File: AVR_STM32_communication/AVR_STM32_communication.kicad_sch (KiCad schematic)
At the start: 124 parts, among them J1 Goldpin_1x3, J2 Conn_01x02_Pin, J3 Conn_01x02_Socket, J4 Goldpin_1x3, J5 Goldpin, J6 Goldpin, J7 Conn_01x02_Pin, Q1 Q_NMOS, Q10 Q_NMOS, Q11 Q_NMOS, Q12 Q_NMOS, Q13 Q_NMOS, Q14 Q_NMOS, Q15 Q_NMOS, Q16 Q_NMOS, Q17 Q_NMOS, Q18 Q_NMOS, Q2 Q_NMOS, Q3 Q_NMOS, Q4 Q_NMOS, Q5 Q_NMOS, Q6 Q_NMOS, Q7 Q_NMOS, Q8 Q_NMOS, Q9 Q_NMOS, SW1 SW_Push, SW2 SW_Push, U1 ATmega328PB-A, U2 ATmega328PB-A, U3 STM32L010C6Tx, Y1 Crystal, Y2 Crystal

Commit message: Dodanie pierwszego STMa, częściowa konfiguracja jego połączeń.
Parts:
- added C7, C8, C9: C, symbol Device:C
- added JP45: Jumper_3_Open, symbol Jumper:Jumper_3_Open
- added JP46, JP47, JP48, JP50: Goldpin+0805, symbol Jumper:Jumper_2_Small_Open
- added R41: 10k, symbol Device:R
- added SW3: SW_Push, symbol Switch:SW_Push
- added Y3: Crystal, symbol Device:Crystal
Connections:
- net +1V8: now also JP46.1 (A)
- net +3V3: now also JP47.1 (A)
- net +3V6: now also JP48.1 (A)
- net GND: now also U3.23 (VSS), U3.35 (VSS), U3.47 (VSS), U3.8 (VSSA), C7.2, C8.2, C9.2, SW3.1
- net at Q18.S, R40.2: now also JP41.3 (B)
- net at JP14.3 (B): now also Q8.S, R18.2
- net at Q7.S, R17.2: now also JP22.3 (B)
- net at Q17.S, R39.2: now also JP40.3 (B)
- net ADC0_STM32_1: now reaches U3.10 (PA0)
- net ADC1_STM32_1: now reaches U3.11 (PA1)
- net RTC_STM32_1: now reaches U3.12 (PA2)
- net TIM2/32-CH4/2_STM32_1: now reaches U3.13 (PA3)
- net GPIO1_STM32_1: now reaches U3.14 (PA4)
- net TIM2_STM32_1: now reaches U3.15 (PA5)
- net VCC_STM32_1: now reaches U3.24 (VDD)
- net VCC_STM32_1: now also U3.36 (VDD), U3.48 (VDD), JP46.2 (B), JP47.2 (B), JP48.2 (B), JP50.1 (A), R41.1
- net EVENTOUT_STM32_1: now reaches U3.29 (PA8)
- net I2C1_SCL_STM32_1: now reaches U3.30 (PA9)
- net I2C1_SDA_STM32_1: now reaches U3.31 (PA10)
- net SWDIO_STM32_1: now reaches U3.34 (PA13)
- net SWCLK_STM32_1: now reaches U3.37 (PA14)
- net USART2_TX_STM32_1: now reaches U3.42 (PB6)
- net at U3.44 (BOOT0): now also JP45.2 (C)
- net OSC1_STM32_1: now reaches U3.5 (PH0)
- net OSC1_STM32_1: now also C7.1, Y3.1
- net OSC2_STM32_1: now reaches U3.6 (PH1)
- net OSC2_STM32_1: now also C8.1, Y3.2
- net RESET_STM32_1: now reaches U3.7 (NRST)
- net RESET_STM32_1: now also C9.1, R41.2, SW3.2
- net at U3.9 (VDDA): now also JP50.2 (B)
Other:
- note added: "CRYSTAL_AVR_1"
- note added: "CRYSTAL_AVR_2"
- note added: "CRYSTAL_STM32_1"
- note added: "RESET_AVR_1"
- note added: "RESET_AVR_2"
- note added: "RESET_STM32_1"
- note added: "UART_AVR_1"
- note added: "UART_AVR_2"
- moved on the sheet: C1, R1, SW1

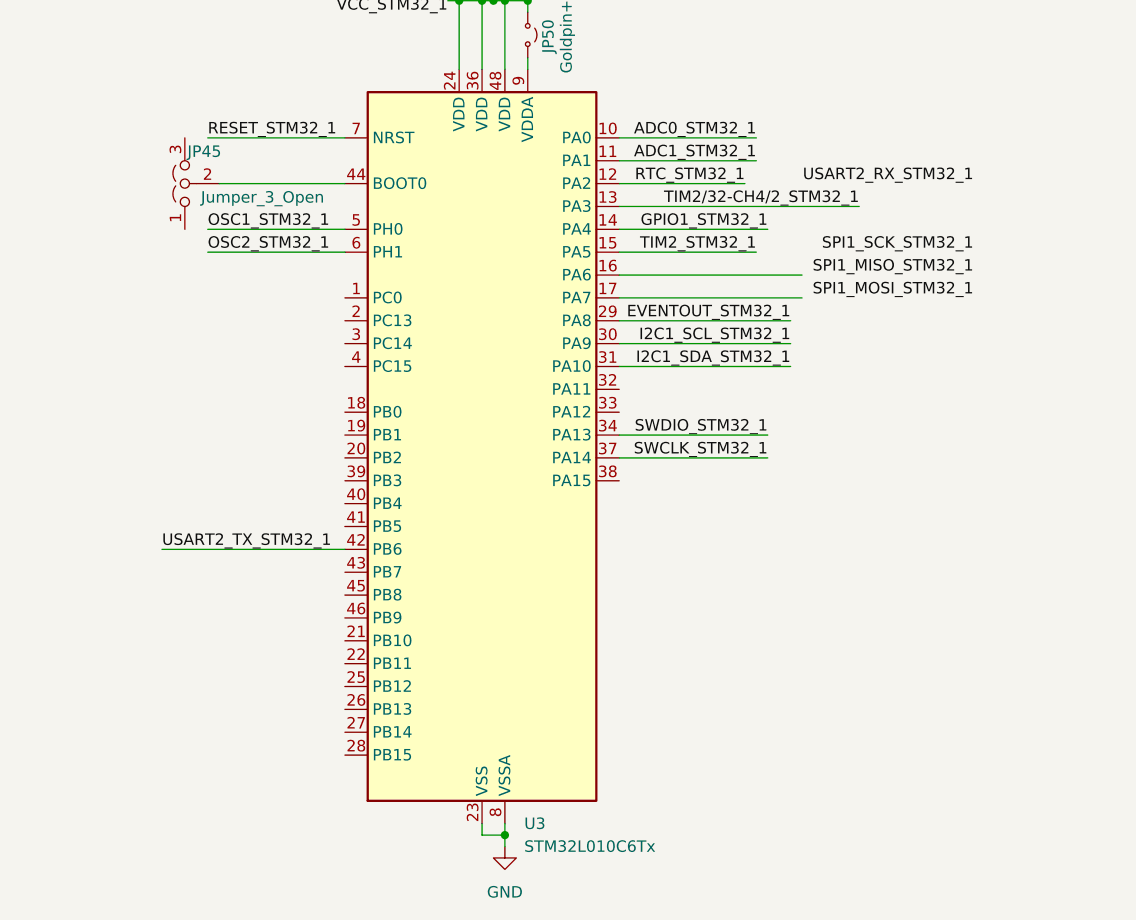
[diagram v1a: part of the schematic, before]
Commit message: Dodanie wszystkich potrzebnych etykiet STM32_1
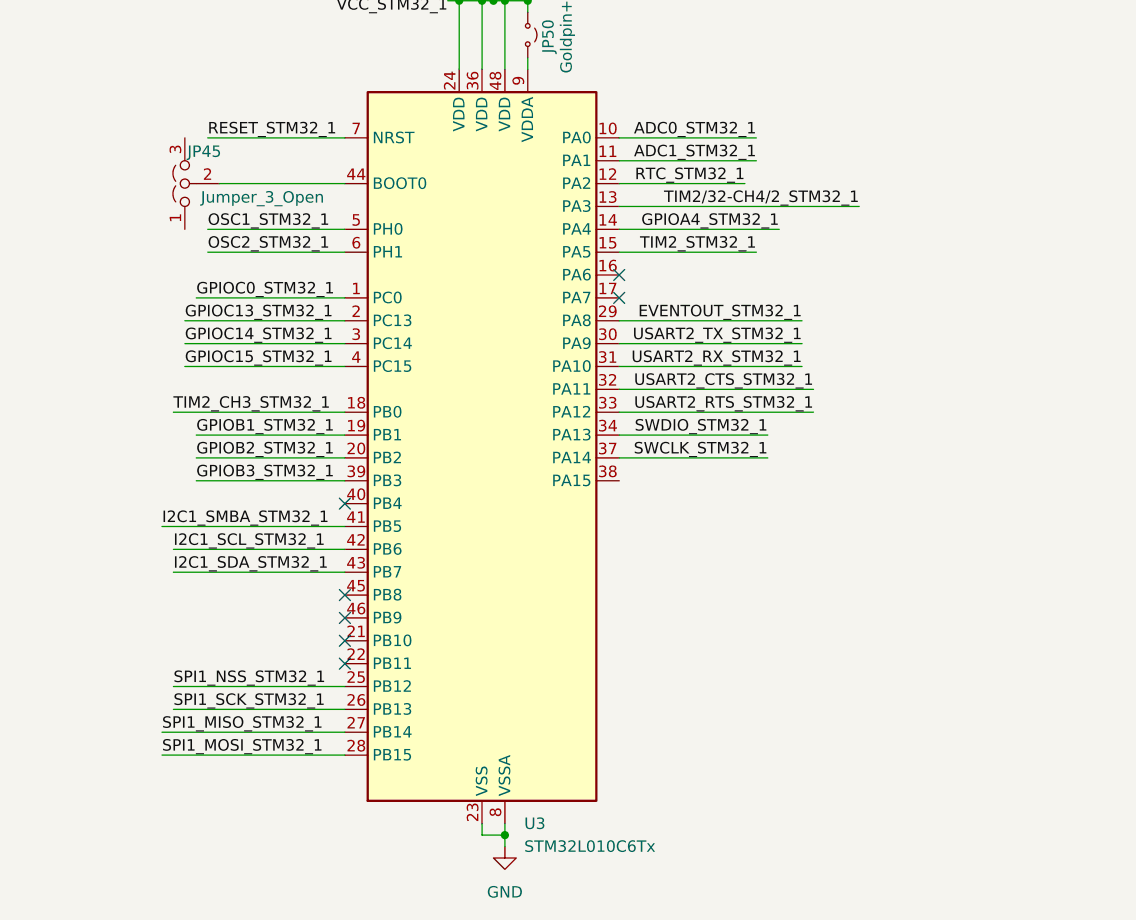
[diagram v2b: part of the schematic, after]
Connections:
- net I2C1_SCL_STM32_1: now also U3.42 (PB6); no longer U3.30 (PA9)
- net I2C1_SDA_STM32_1: now also U3.43 (PB7); no longer U3.31 (PA10)
- net SPI1_MISO_STM32_1: now also U3.27 (PB14)
- net SPI1_MOSI_STM32_1: now also U3.28 (PB15)
- net SPI1_SCK_STM32_1: now also U3.26 (PB13)
- net USART2_RX_STM32_1: now also U3.31 (PA10)
- net USART2_TX_STM32_1: now also U3.30 (PA9); no longer U3.42 (PB6)
- net GPIOC0_STM32_1: now reaches U3.1 (PC0)
- net TIM2_CH3_STM32_1: now reaches U3.18 (PB0)
- net GPIOB1_STM32_1: now reaches U3.19 (PB1)
- net GPIOC13_STM32_1: now reaches U3.2 (PC13)
- net GPIOB2_STM32_1: now reaches U3.20 (PB2)
- net SPI1_NSS_STM32_1: now reaches U3.25 (PB12)
- net GPIOC14_STM32_1: now reaches U3.3 (PC14)
- net USART2_CTS_STM32_1: now reaches U3.32 (PA11)
- net USART2_RTS_STM32_1: now reaches U3.33 (PA12)
- net GPIOB3_STM32_1: now reaches U3.39 (PB3)
- net GPIOC15_STM32_1: now reaches U3.4 (PC15)
- net I2C1_SMBA_STM32_1: now reaches U3.41 (PB5)
- net GPIO1_STM32_1 renamed GPIOA4_STM32_1
- no-connect marks 0 -> 7

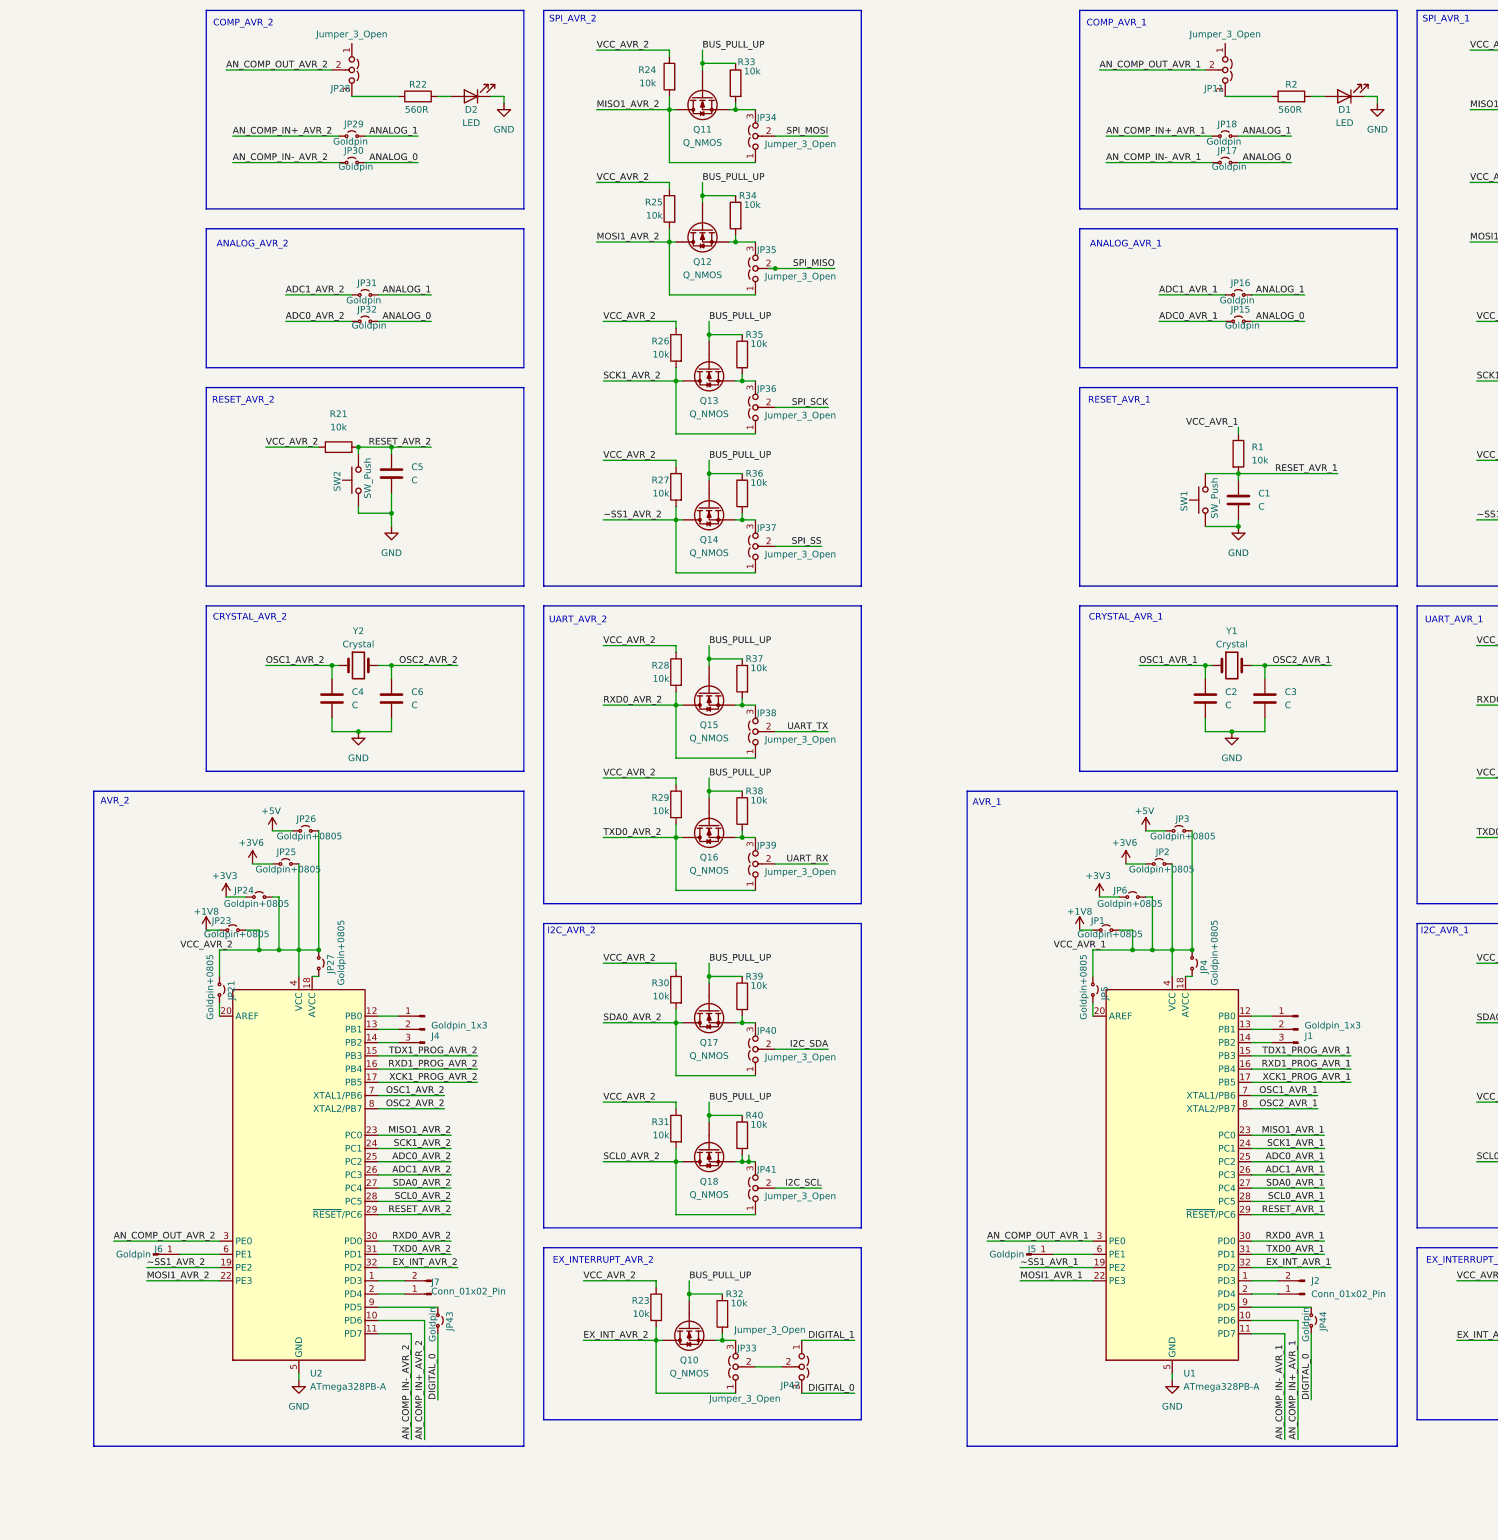
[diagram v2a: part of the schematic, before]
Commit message: Poprawa ułożenia etykiet w AVR
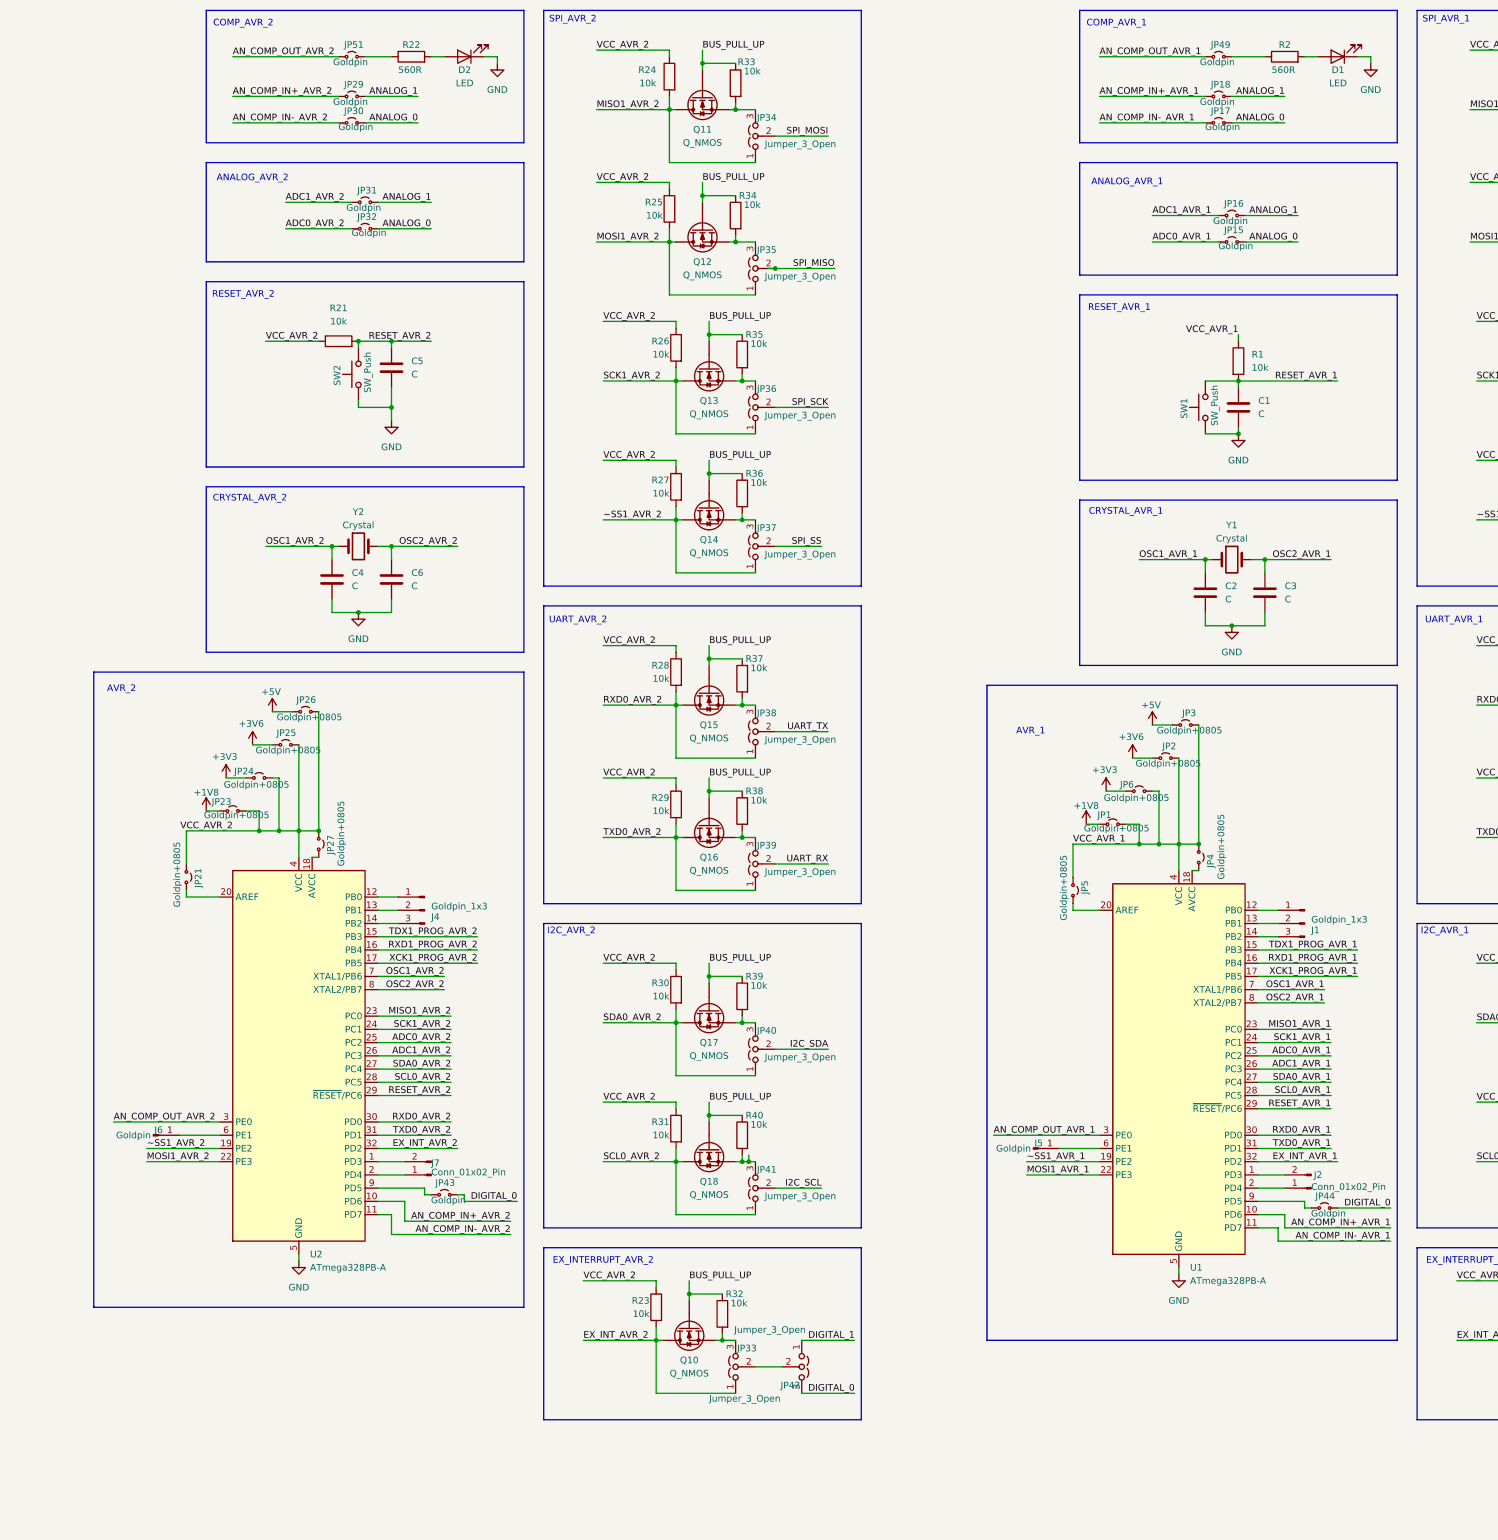
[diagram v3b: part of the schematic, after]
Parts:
- removed JP11, JP28: Jumper_3_Open, symbol Jumper:Jumper_3_Open
- added JP49, JP51: Goldpin, symbol Jumper:Jumper_2_Small_Open
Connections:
- net AN_COMP_OUT_AVR_1: now also JP49.1 (A)
- net AN_COMP_OUT_AVR_2: now also JP51.1 (A)
- net at R2.1: now also JP49.2 (B)
- net at R22.1: now also JP51.2 (B)
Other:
- moved on the sheet: C1, C2, C3, C4, C5, C6, D1, D2, J1, J2, J4, J5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

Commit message: Wydzielenie sekcji zasilania obu AVR jako oddzielny moduł.
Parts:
- removed JP23, JP24, JP25, JP26: Goldpin+0805, symbol Jumper:Jumper_2_Small_Open
- added JP11, JP28, JP52, JP53, JP54, JP55, JP56, JP57: Goldpin+0805, symbol Jumper:Jumper_2_Small_Open
- JP45: value Jumper_3_Open -> Goldpin+0805
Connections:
- net +1V8: now also JP11.1 (A), JP54.1 (A)
- net +3V3: now also JP53.1 (A), JP57.1 (A)
- net +3V6: now also JP52.1 (A), JP56.1 (A)
- net +5V: now also JP28.1 (A), JP55.1 (A)
- net GND: now also JP45.1 (A)
- net VCC_AVR_2: now also JP11.2 (B), JP28.2 (B), JP52.2 (B), JP53.2 (B), JP54.2 (B), JP55.2 (B), JP56.2 (B), JP57.2 (B)
- net VCC_STM32_1: now also JP45.3 (B)
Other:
- note added: "STM32_1"
- note added: "VCC_AVR_1"
- note added: "VCC_AVR_2"
- moved on the sheet: C1, C2, C3, C4, C5, C6, D1, D2, J1, J2, J4, J5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
